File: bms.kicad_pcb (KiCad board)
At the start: 2 copper layers, 252 x 136.7 mm, 214 parts, among them J1501 CONN_01X02, J1502 CONN_01X02, J201 CONN_01X02, J202 CONN_01X02, P1001 CONN_01X01, P1101 CONN_01X01, P1201 CONN_01X01, P1301 CONN_01X01, P1401 CONN_01X01, P1501 CONN_01X01, P1601 CONN_01X01, P1701 CONN_01X01, P1801 CONN_01X01, P1901 CONN_01X01, P2001 CONN_01X01, P201 CONN_01X01, P2101 CONN_01X01, P2201 CONN_01X01, P2301 CONN_01X01, P2401 CONN_01X01, P2501 CONN_01X01, P2601 CONN_01X01, P2701 CONN_01X01, P301 CONN_01X01, P401 CONN_01X01, P501 CONN_01X01, P601 CONN_01X01, P701 CONN_01X01, P801 CONN_01X01, P901 CONN_01X01, Q1001 DMP3130LQ, Q1101 DMP3130LQ, Q1201 DMP3130LQ, Q1301 DMP3130LQ, Q1401 DMP3130LQ, Q1501 NSV1C201MZ4, Q1601 DMP3130LQ, Q1701 DMP3130LQ, Q1801 DMP3130LQ, Q1901 DMP3130LQ, Q2001 DMP3130LQ, Q201 NSV1C201MZ4, Q2101 DMP3130LQ, Q2201 DMP3130LQ, Q2301 DMP3130LQ, Q2401 DMP3130LQ, Q2501 DMP3130LQ, Q2601 DMP3130LQ, Q2701 DMP3130LQ, Q301 DMP3130LQ, Q401 DMP3130LQ, Q501 DMP3130LQ, Q601 DMP3130LQ, Q701 DMP3130LQ, Q801 DMP3130LQ, Q901 DMP3130LQ, T1501 HX0068ANL, T201 HX0068ANL, U1501 LTC6804-1, U201 LTC6804-1

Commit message: Place balance wire solder points for pack A
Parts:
- P1001, P1101, P1201, P1301, P1401, P1501, P1601, P1701, P1801, P1901, P2001, P201, P2101, P2201, P2301, P2401, P2501, P2601, P2701, P301, P401, P501, P601, P701, P801, P901: footprint Measurement_Points:Test_Point_Keystone_5015_Micro-Minature -> bms:Solder_Point_Round-TH_0.5mm
- moved C1201 418.7 mm to (-115.6, 125.2)
- moved C401 418.7 mm to (-86.8, 142.8)
- moved C701 418.7 mm to (-86.8, 125.2)
- moved C801 418.7 mm to (-115.6, 142.8)
- moved Q1201 418.7 mm to (-124.0, 123.9)
- moved Q301 418.7 mm to (-66.4, 123.9)
- moved Q401 418.7 mm to (-95.2, 141.4)
- moved Q701 418.7 mm to (-95.2, 123.9)
- moved Q801 418.7 mm to (-124.0, 141.4)
- moved R1203 418.7 mm to (-109.2, 125.2)
- moved R301 418.7 mm to (-56.8, 118.2)
- moved R302 418.7 mm to (-52.1, 125.2)
- moved R303 418.7 mm to (-50.5, 117.0)
- moved R401 418.7 mm to (-85.6, 135.7)
- moved R403 418.7 mm to (-80.9, 142.8)
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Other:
- board text added: "pack +"
- board text added: "pack -"

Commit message: very rough placement of cell subcircuits
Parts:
- C1001, C1101, C1201, C1301, C1401, C1506, C1507, C1601, C1701, C1801, C1901, C2001, C206, C207, C2101, C2201, C2301, C2401, C2501, C2601, C2701, C301, C401, C501, C601, C701, C801, C901: footprint Capacitors_SMD:C_0603 -> Capacitors_SMD:C_0402
- R1002, R1003, R1102, R1103, R1202, R1203, R1302, R1303, R1402, R1403, R1504, R1507, R1508, R1509, R1510, R1511, R1512, R1513, R1514, R1515, R1602, R1603, R1702, R1703, R1802, R1803, R1902, R1903, R2002, R2003, R204, R207, R208, R209, R210, R2102, R2103, R211, R212, R213, R214, R215, R2202, R2203, R2302, R2303, R2402, R2403, R2502, R2503, R2602, R2603, R2702, R2703, R302, R303, R402, R403, R502, R503, R602, R603, R702, R703, R802, R803, R902, R903: footprint Resistors_SMD:R_0603 -> Resistors_SMD:R_0402
- moved C401 341.1 mm to (254.2, 150.8)
- moved Q401 341.1 mm to (245.8, 149.4)
- moved R401 341.1 mm to (255.4, 143.7)
- moved R402 341.1 mm to (261.6, 142.5)
- moved R403 341.1 mm to (260.1, 150.8)
- moved Q301 337.6 mm to (270.0, 95.0), turned to 90 degrees
- moved R301 321.5 mm to (264.2, 100.2)
- moved R302 321.5 mm to (268.9, 107.2)
- moved R303 321.5 mm to (270.5, 99.0)
- moved C801 287.1 mm to (171.4, 150.8)
- moved Q801 287.1 mm to (163.0, 149.4)
- moved R801 287.1 mm to (172.5, 143.7)
- moved R802 287.1 mm to (177.3, 150.8)
- moved R803 287.1 mm to (178.8, 142.5)
- moved C1501 280.2 mm to (146.2, -46.4)
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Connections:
- J1501 pad 1: /PackB/isoSPIB+ -> /isoSPI_P2P_+
- J1501 pad 2: /PackB/isoSPIB- -> /isoSPI_P2P_-
- J201 pad 1: /PackB/isoSPIA+ -> /PackA/isoSPIB+
- J201 pad 2: /PackB/isoSPIA- -> /PackA/isoSPIB-
- J202 pad 1: /PackA/isoSPIA+ -> /isoSPI_P2P_+
- J202 pad 2: /PackA/isoSPIA- -> /isoSPI_P2P_-
- R1001 pad 2: (no net) -> /PackA/Cell4/Cell+
- R1101 pad 2: (no net) -> /PackA/Cell3/Cell+
- R1201 pad 2: (no net) -> /PackA/Cell2/Cell+
- R1301 pad 2: (no net) -> /PackA/Cell1/Cell+
- R1601 pad 2: (no net) -> /PackB/Cell11/Cell+
- R1701 pad 2: (no net) -> /PackB/Cell10/Cell+
- R1801 pad 2: (no net) -> /PackB/Cell9/Cell+
- R1901 pad 2: (no net) -> /PackB/Cell8/Cell+
- R2001 pad 2: (no net) -> /PackB/Cell7/Cell+
- R2101 pad 2: (no net) -> /PackB/Cell6/Cell+
- R2201 pad 2: (no net) -> /PackB/Cell5/Cell+
- R2301 pad 2: (no net) -> /PackB/Cell4/Cell+
- R2401 pad 2: (no net) -> /PackB/Cell3/Cell+
- R2501 pad 2: (no net) -> /PackB/Cell2/Cell+
- R2601 pad 2: (no net) -> /PackB/Cell1/Cell+
- R301 pad 2: (no net) -> /PackA/Cell11/Cell+
- R401 pad 2: (no net) -> /PackA/Cell10/Cell+
- R501 pad 2: (no net) -> /PackA/Cell9/Cell+
- R601 pad 2: (no net) -> /PackA/Cell8/Cell+
- R701 pad 2: (no net) -> /PackA/Cell7/Cell+
- R801 pad 2: (no net) -> /PackA/Cell6/Cell+
- R901 pad 2: (no net) -> /PackA/Cell5/Cell+
- T1501 pad 5: /PackB/isoSPIB+ -> /isoSPI_P2P_+
- T1501 pad 6: /PackB/isoSPIB- -> /isoSPI_P2P_-
- T201 pad 1: /PackA/isoSPIA+ -> /isoSPI_P2P_+
- T201 pad 2: /PackA/isoSPIA- -> /isoSPI_P2P_-
- T201 pad 5: /PackB/isoSPIA+ -> /PackA/isoSPIB+
- T201 pad 6: /PackB/isoSPIA- -> /PackA/isoSPIB-
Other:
- outline, holes or cut-outs redrawn

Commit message: place and route filter caps
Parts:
- moved R302 111.1 mm to (158.3, 116.9)
- moved R402 106.8 mm to (158.3, 115.6)
- moved C401 104.5 mm to (155.5, 116.3), turned to 270 degrees
- moved C1301 78.9 mm to (144.7, 116.3), turned to 90 degrees
- moved R502 78.5 mm to (156.1, 114.2), turned to 90 degrees
- moved R602 71.8 mm to (154.3, 114.2), turned to 90 degrees
- moved C1201 68.7 mm to (145.9, 116.3), turned to 270 degrees
- moved C601 66.7 mm to (153.1, 116.3), turned to 270 degrees
- moved C1101 43.5 mm to (147.1, 116.3), turned to 90 degrees
- moved C701 42.1 mm to (151.9, 116.3), turned to 90 degrees
- moved C801 40.2 mm to (150.7, 116.3), turned to 270 degrees
- moved C1001 39.3 mm to (148.3, 116.3), turned to 270 degrees
- moved C901 14.6 mm to (149.5, 116.3), turned to 90 degrees
- moved R301 2.29 mm to (265.0, 98.0), turned to 270 degrees
- moved C301 1.48 mm to (156.7, 116.3), turned to 90 degrees
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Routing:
- net /PackA/C11: track 0.00 -> 4.56 mm
- net /PackA/C3: track 0.00 -> 4.53 mm
- net /PackA/C9: track 0.00 -> 4.15 mm
- net /PackA/C5: track 0.00 -> 4.11 mm
- net /PackA/C1: track 0.00 -> 4.10 mm
- net /PackA/C7: track 0.00 -> 3.96 mm
- net /PackA/C12: track 0.00 -> 3.60 mm
- net /PackA/C2: track 0.00 -> 3.57 mm
- net /PackA/C10: track 0.00 -> 3.40 mm
- net /PackA/C4: track 0.00 -> 3.23 mm
- net /PackA/C8: track 0.00 -> 3.00 mm
- net /PackA/C6: track 0.00 -> 2.93 mm
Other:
- net class Default: clearance 0.2 -> 0.1778; trace_width 0.25 -> 0.1778; via_dia 0.6 -> 0.381; via_drill 0.4 -> 0.2286
- rule pad_to_mask_clearance: 0.2 -> 0.14
- rule trace_clearance: 0.2 -> 0.1778
- rule trace_min: 0.2 -> 0.127
- rule via_min_drill: 0.3 -> 0.2032
- rule via_min_size: 0.4 -> 0.3302

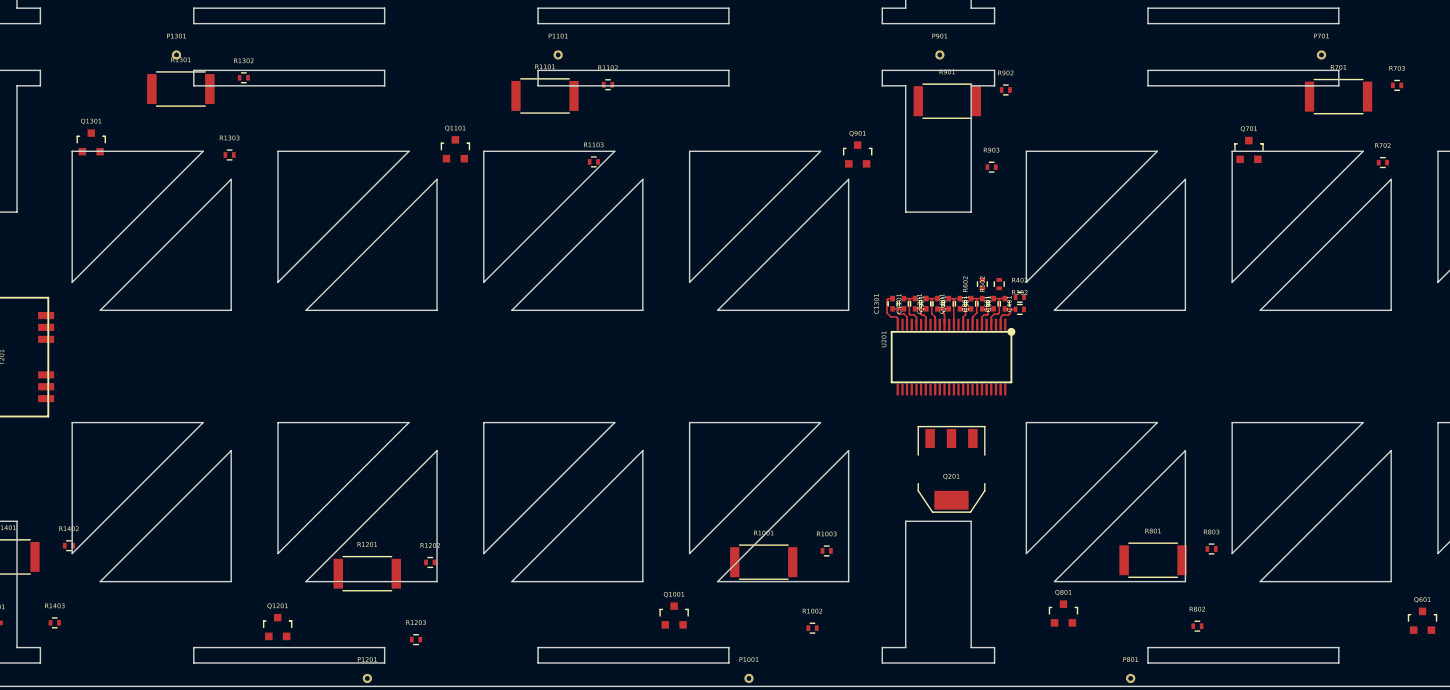
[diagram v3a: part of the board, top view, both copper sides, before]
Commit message: place RC filter resistors
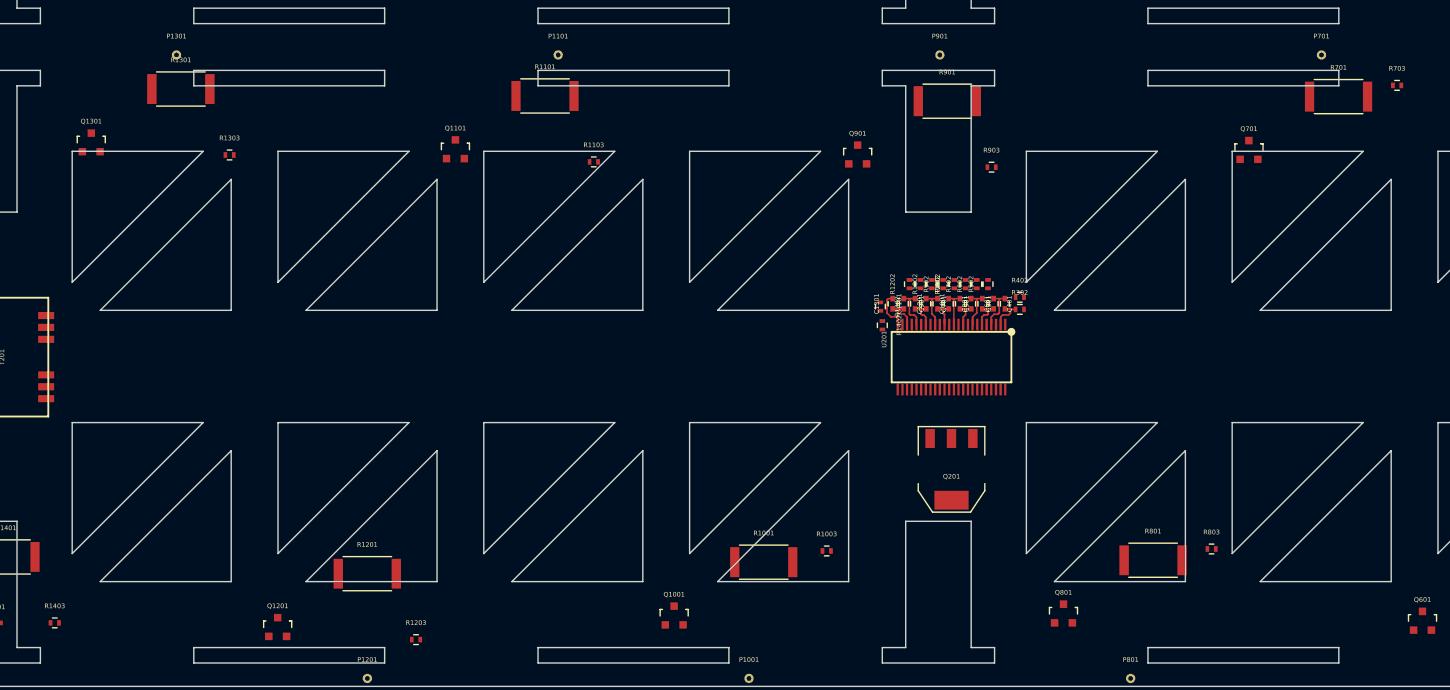
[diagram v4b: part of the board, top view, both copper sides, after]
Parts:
- moved R1402 90.1 mm to (143.6, 118.6), turned to 270 degrees
- moved R1302 72.3 mm to (143.4, 116.6), turned to 270 degrees
- moved R1202 59.2 mm to (146.5, 114.2), turned to 90 degrees
- moved R702 46.5 mm to (152.5, 114.2), turned to 90 degrees
- moved R802 44.9 mm to (151.3, 114.2), turned to 90 degrees
- moved R1102 39.6 mm to (147.7, 114.2), turned to 270 degrees
- moved R1002 38.9 mm to (148.9, 114.2), turned to 90 degrees
- moved R902 21.8 mm to (150.1, 114.2), turned to 90 degrees
- moved R502 1.20 mm to (154.9, 114.2)
- moved R602 0.60 mm to (153.7, 114.2)
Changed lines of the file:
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@@
   (general
     (links 358)
-    (no_connects 342)
+    (no_connects 335)
     (area 23.524999 20.424999 275.675001 157.275001)
     (thickness 1.6)
@@
     (45 Margin user)
     (46 B.CrtYd user)
-    (47 F.CrtYd user hide)
+    (47 F.CrtYd user)
     (48 B.Fab user)
     (49 F.Fab user)
@@
   )
   (module Resistors_SMD:R_0402 (layer F.Cu)
-    (at 156.1 114.2 90)
+    (at 154.9 114.2 90)
     (descr "Resistor SMD 0402, reflow soldering, Vishay (see dcrcw.pdf)")
     (tags "resistor 0402")
@@
   )
   (module Resistors_SMD:R_0402 (layer F.Cu)
-    (at 154.3 114.2 90)
+    (at 153.7 114.2 90)
     (descr "Resistor SMD 0402, reflow soldering, Vishay (see dcrcw.pdf)")
     (tags "resistor 0402")
@@
   )
   (module Resistors_SMD:R_0402 (layer F.Cu)
-    (at 197.110571 101.203)
+    (at 152.5 114.2 90)
     (descr "Resistor SMD 0402, reflow soldering, Vishay (see dcrcw.pdf)")
     (tags "resistor 0402")
     (attr smd)
-    (fp_text reference R702 (at 0 -1.8) (layer F.SilkS)
+    (fp_text reference R702 (at 0 -1.8 90) (layer F.SilkS)
       (effects (font (size 0.5 0.5) (thickness 0.11)))
     )
-    (fp_text value 100 (at 0 1.8) (layer F.Fab)
+    (fp_text value 100 (at 0 1.8 90) (layer F.Fab)
       (effects (font (size 1 1) (thickness 0.15)))
     )
@@
     (fp_line (start 0.25 -0.525) (end -0.25 -0.525) (layer F.SilkS) (width 0.15))
     (fp_line (start -0.25 0.525) (end 0.25 0.525) (layer F.SilkS) (width 0.15))
-    (pad 1 smd rect (at -0.45 0) (size 0.4 0.6) (layers F.Cu F.Paste F.Mask)
+    (pad 1 smd rect (at -0.45 0 90) (size 0.4 0.6) (layers F.Cu F.Paste F.Mask)
       (net 14 /PackA/C8))
-    (pad 2 smd rect (at 0.45 0) (size 0.4 0.6) (layers F.Cu F.Paste F.Mask)
+    (pad 2 smd rect (at 0.45 0 90) (size 0.4 0.6) (layers F.Cu F.Paste F.Mask)
       (net 53 /PackA/Cell8/Cell+))
     (model Resistors_SMD.3dshapes/R_0402.wrl
@@
   )
   (module Resistors_SMD:R_0402 (layer F.Cu)
-    (at 177.280571 150.763)
+    (at 151.3 114.2 90)
     (descr "Resistor SMD 0402, reflow soldering, Vishay (see dcrcw.pdf)")
     (tags "resistor 0402")
     (attr smd)
-    (fp_text reference R802 (at 0 -1.8) (layer F.SilkS)
+    (fp_text reference R802 (at 0 -1.8 90) (layer F.SilkS)
       (effects (font (size 0.5 0.5) (thickness 0.11)))
     )
-    (fp_text value 100 (at 0 1.8) (layer F.Fab)
+    (fp_text value 100 (at 0 1.8 90) (layer F.Fab)
       (effects (font (size 1 1) (thickness 0.15)))
     )
@@
     (fp_line (start 0.25 -0.525) (end -0.25 -0.525) (layer F.SilkS) (width 0.15))
     (fp_line (start -0.25 0.525) (end 0.25 0.525) (layer F.SilkS) (width 0.15))
-    (pad 1 smd rect (at -0.45 0) (size 0.4 0.6) (layers F.Cu F.Paste F.Mask)
+    (pad 1 smd rect (at -0.45 0 90) (size 0.4 0.6) (layers F.Cu F.Paste F.Mask)
       (net 15 /PackA/C7))
-    (pad 2 smd rect (at 0.45 0) (size 0.4 0.6) (layers F.Cu F.Paste F.Mask)
+    (pad 2 smd rect (at 0.45 0 90) (size 0.4 0.6) (layers F.Cu F.Paste F.Mask)
       (net 54 /PackA/Cell7/Cell+))
     (model Resistors_SMD.3dshapes/R_0402.wrl
@@
   )
   (module Resistors_SMD:R_0402 (layer F.Cu)
-    (at 156.800571 93.443)
+    (at 150.1 114.2 90)
     (descr "Resistor SMD 0402, reflow soldering, Vishay (see dcrcw.pdf)")
     (tags "resistor 0402")
     (attr smd)
-    (fp_text reference R902 (at 0 -1.8) (layer F.SilkS)
+    (fp_text reference R902 (at 0 -1.8 90) (layer F.SilkS)
       (effects (font (size 0.5 0.5) (thickness 0.11)))
     )
-    (fp_text value 100 (at 0 1.8) (layer F.Fab)
+    (fp_text value 100 (at 0 1.8 90) (layer F.Fab)
       (effects (font (size 1 1) (thickness 0.15)))
     )
@@
     (fp_line (start 0.25 -0.525) (end -0.25 -0.525) (layer F.SilkS) (width 0.15))
     (fp_line (start -0.25 0.525) (end 0.25 0.525) (layer F.SilkS) (width 0.15))
-    (pad 1 smd rect (at -0.45 0) (size 0.4 0.6) (layers F.Cu F.Paste F.Mask)
+    (pad 1 smd rect (at -0.45 0 90) (size 0.4 0.6) (layers F.Cu F.Paste F.Mask)
       (net 16 /PackA/C6))
-    (pad 2 smd rect (at 0.45 0) (size 0.4 0.6) (layers F.Cu F.Paste F.Mask)
+    (pad 2 smd rect (at 0.45 0 90) (size 0.4 0.6) (layers F.Cu F.Paste F.Mask)
       (net 55 /PackA/Cell6/Cell+))
     (model Resistors_SMD.3dshapes/R_0402.wrl
@@
   )
   (module Resistors_SMD:R_0402 (layer F.Cu)
-    (at 136.136762 150.973)
+    (at 148.9 114.2 90)
     (descr "Resistor SMD 0402, reflow soldering, Vishay (see dcrcw.pdf)")
     (tags "resistor 0402")
     (attr smd)
-    (fp_text reference R1002 (at 0 -1.8) (layer F.SilkS)
+    (fp_text reference R1002 (at 0 -1.8 90) (layer F.SilkS)
       (effects (font (size 0.5 0.5) (thickness 0.11)))
     )
-    (fp_text value 100 (at 0 1.8) (layer F.Fab)
+    (fp_text value 100 (at 0 1.8 90) (layer F.Fab)
       (effects (font (size 1 1) (thickness 0.15)))
     )
@@
     (fp_line (start 0.25 -0.525) (end -0.25 -0.525) (layer F.SilkS) (width 0.15))
     (fp_line (start -0.25 0.525) (end 0.25 0.525) (layer F.SilkS) (width 0.15))
-    (pad 1 smd rect (at -0.45 0) (size 0.4 0.6) (layers F.Cu F.Paste F.Mask)
+    (pad 1 smd rect (at -0.45 0 90) (size 0.4 0.6) (layers F.Cu F.Paste F.Mask)
       (net 17 /PackA/C5))
-    (pad 2 smd rect (at 0.45 0) (size 0.4 0.6) (layers F.Cu F.Paste F.Mask)
+    (pad 2 smd rect (at 0.45 0 90) (size 0.4 0.6) (layers F.Cu F.Paste F.Mask)
       (net 56 /PackA/Cell5/Cell+))
     (model Resistors_SMD.3dshapes/R_0402.wrl
@@
   )
   (module Resistors_SMD:R_0402 (layer F.Cu)
-    (at 114.276762 92.883)
+    (at 147.7 114.2 270)
     (descr "Resistor SMD 0402, reflow soldering, Vishay (see dcrcw.pdf)")
     (tags "resistor 0402")
     (attr smd)
-    (fp_text reference R1102 (at 0 -1.8) (layer F.SilkS)
+    (fp_text reference R1102 (at 0 -1.8 270) (layer F.SilkS)
       (effects (font (size 0.5 0.5) (thickness 0.11)))
     )
-    (fp_text value 100 (at 0 1.8) (layer F.Fab)
+    (fp_text value 100 (at 0 1.8 270) (layer F.Fab)
       (effects (font (size 1 1) (thickness 0.15)))
     )
@@
     (fp_line (start 0.25 -0.525) (end -0.25 -0.525) (layer F.SilkS) (width 0.15))
     (fp_line (start -0.25 0.525) (end 0.25 0.525) (layer F.SilkS) (width 0.15))
-    (pad 1 smd rect (at -0.45 0) (size 0.4 0.6) (layers F.Cu F.Paste F.Mask)
+    (pad 1 smd rect (at -0.45 0 270) (size 0.4 0.6) (layers F.Cu F.Paste F.Mask)
       (net 18 /PackA/C4))
-    (pad 2 smd rect (at 0.45 0) (size 0.4 0.6) (layers F.Cu F.Paste F.Mask)
+    (pad 2 smd rect (at 0.45 0 270) (size 0.4 0.6) (layers F.Cu F.Paste F.Mask)
       (net 57 /PackA/Cell4/Cell+))
     (model Resistors_SMD.3dshapes/R_0402.wrl
@@
   )
   (module Resistors_SMD:R_0402 (layer F.Cu)
-    (at 95.276762 143.953)
+    (at 146.5 114.2 90)
     (descr "Resistor SMD 0402, reflow soldering, Vishay (see dcrcw.pdf)")
     (tags "resistor 0402")
     (attr smd)
-    (fp_text reference R1202 (at 0 -1.8) (layer F.SilkS)
+    (fp_text reference R1202 (at 0 -1.8 90) (layer F.SilkS)
       (effects (font (size 0.5 0.5) (thickness 0.11)))
     )
-    (fp_text value 100 (at 0 1.8) (layer F.Fab)
+    (fp_text value 100 (at 0 1.8 90) (layer F.Fab)
       (effects (font (size 1 1) (thickness 0.15)))
     )
@@
     (fp_line (start 0.25 -0.525) (end -0.25 -0.525) (layer F.SilkS) (width 0.15))
     (fp_line (start -0.25 0.525) (end 0.25 0.525) (layer F.SilkS) (width 0.15))
-    (pad 1 smd rect (at -0.45 0) (size 0.4 0.6) (layers F.Cu F.Paste F.Mask)
+    (pad 1 smd rect (at -0.45 0 90) (size 0.4 0.6) (layers F.Cu F.Paste F.Mask)
       (net 19 /PackA/C3))
-    (pad 2 smd rect (at 0.45 0) (size 0.4 0.6) (layers F.Cu F.Paste F.Mask)
+    (pad 2 smd rect (at 0.45 0 90) (size 0.4 0.6) (layers F.Cu F.Paste F.Mask)
       (net 58 /PackA/Cell3/Cell+))
     (model Resistors_SMD.3dshapes/R_0402.wrl
@@
   )
   (module Resistors_SMD:R_0402 (layer F.Cu)
-    (at 75.346762 92.143)
+    (at 143.4 116.6 270)
     (descr "Resistor SMD 0402, reflow soldering, Vishay (see dcrcw.pdf)")
     (tags "resistor 0402")
     (attr smd)
-    (fp_text reference R1302 (at 0 -1.8) (layer F.SilkS)
+    (fp_text reference R1302 (at 0 -1.8 270) (layer F.SilkS)
       (effects (font (size 0.5 0.5) (thickness 0.11)))
     )
-    (fp_text value 100 (at 0 1.8) (layer F.Fab)
+    (fp_text value 100 (at 0 1.8 270) (layer F.Fab)
       (effects (font (size 1 1) (thickness 0.15)))
     )
@@
     (fp_line (start 0.25 -0.525) (end -0.25 -0.525) (layer F.SilkS) (width 0.15))
     (fp_line (start -0.25 0.525) (end 0.25 0.525) (layer F.SilkS) (width 0.15))
-    (pad 1 smd rect (at -0.45 0) (size 0.4 0.6) (layers F.Cu F.Paste F.Mask)
+    (pad 1 smd rect (at -0.45 0 270) (size 0.4 0.6) (layers F.Cu F.Paste F.Mask)
       (net 20 /PackA/C2))
-    (pad 2 smd rect (at 0.45 0) (size 0.4 0.6) (layers F.Cu F.Paste F.Mask)
+    (pad 2 smd rect (at 0.45 0 270) (size 0.4 0.6) (layers F.Cu F.Paste F.Mask)
       (net 59 /PackA/Cell2/Cell+))
     (model Resistors_SMD.3dshapes/R_0402.wrl
@@
   )
   (module Resistors_SMD:R_0402 (layer F.Cu)
-    (at 56.656762 142.163)
+    (at 143.6 118.6 270)
     (descr "Resistor SMD 0402, reflow soldering, Vishay (see dcrcw.pdf)")
     (tags "resistor 0402")
     (attr smd)
-    (fp_text reference R1402 (at 0 -1.8) (layer F.SilkS)
+    (fp_text reference R1402 (at 0 -1.8 270) (layer F.SilkS)
       (effects (font (size 0.5 0.5) (thickness 0.11)))
     )
-    (fp_text value 100 (at 0 1.8) (layer F.Fab)
+    (fp_text value 100 (at 0 1.8 270) (layer F.Fab)
       (effects (font (size 1 1) (thickness 0.15)))
     )
@@
     (fp_line (start 0.25 -0.525) (end -0.25 -0.525) (layer F.SilkS) (width 0.15))
     (fp_line (start -0.25 0.525) (end 0.25 0.525) (layer F.SilkS) (width 0.15))
-    (pad 1 smd rect (at -0.45 0) (size 0.4 0.6) (layers F.Cu F.Paste F.Mask)
+    (pad 1 smd rect (at -0.45 0 270) (size 0.4 0.6) (layers F.Cu F.Paste F.Mask)
       (net 21 /PackA/C1))
-    (pad 2 smd rect (at 0.45 0) (size 0.4 0.6) (layers F.Cu F.Paste F.Mask)
+    (pad 2 smd rect (at 0.45 0 270) (size 0.4 0.6) (layers F.Cu F.Paste F.Mask)
       (net 60 /PackA/Cell1/Cell+))
     (model Resistors_SMD.3dshapes/R_0402.wrl

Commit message: placement progress
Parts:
- R1501, R201: footprint Resistors_SMD:R_0603 -> Resistors_SMD:R_0402
- moved J202 222.3 mm to (258.9, 129.3), turned to 90 degrees
- moved J201 222.2 mm to (258.9, 118.3), turned to 90 degrees
- moved T201 196.0 mm to (245.9, 124.3), turned to 90 degrees
- moved C1401 98.5 mm to (143.6, 124.0), turned to 270 degrees
- moved R205 66.6 mm to (158.5, 126.1), turned to 90 degrees
- moved R201 56.5 mm to (143.3, 125.9)
- moved R207 55.5 mm to (151.4, 127.2), turned to 270 degrees
- moved C205 51.8 mm to (149.3, 128.5), turned to 180 degrees
- moved R208 50.1 mm to (152.7, 127.2), turned to 270 degrees
- moved C202 47.5 mm to (149.3, 127.0), turned to 180 degrees
- moved R206 45.0 mm to (154.7, 127.1)
- moved C203 33.4 mm to (147.0, 132.2), turned to 90 degrees
- moved Q201 0.73 mm to (151.7, 134.2)
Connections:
- J1501 pad 1: /isoSPI_P2P_+ -> /PackB/isoSPIB+
- J1501 pad 2: /isoSPI_P2P_- -> /PackB/isoSPIB-
- J1502 pad 1: /PackB/isoSPIA+ -> /isoSPI_P2P_+
- J1502 pad 2: /PackB/isoSPIA- -> /isoSPI_P2P_-
- J201 pad 1: /PackA/isoSPIB+ -> /isoSPI_P2P_+
- J201 pad 2: /PackA/isoSPIB- -> /isoSPI_P2P_-
- J202 pad 1: /isoSPI_P2P_+ -> /PackA/isoSPIA+
- J202 pad 2: /isoSPI_P2P_- -> /PackA/isoSPIA-
- T1501 pad 1: /PackB/isoSPIA+ -> /isoSPI_P2P_+
- T1501 pad 2: /PackB/isoSPIA- -> /isoSPI_P2P_-
- T1501 pad 5: /isoSPI_P2P_+ -> /PackB/isoSPIB+
- T1501 pad 6: /isoSPI_P2P_- -> /PackB/isoSPIB-
- T201 pad 1: /isoSPI_P2P_+ -> /PackA/isoSPIA+
- T201 pad 2: /isoSPI_P2P_- -> /PackA/isoSPIA-
- T201 pad 5: /PackA/isoSPIB+ -> /isoSPI_P2P_+
- T201 pad 6: /PackA/isoSPIB- -> /isoSPI_P2P_-
